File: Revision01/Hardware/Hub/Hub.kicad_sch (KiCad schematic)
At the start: 25 parts, among them J20 Conn_01x04, J3 Conn_01x04, J4 Conn_01x05, J5 Conn_01x05, SW1 ON/OFF_SW_SPST_LED, U1 NUCLEO-L476RG, U2 LMR51603XFDBVR

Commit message: . Fixed major BOM bug in Antenna, ordering correct Male Outer, Male Inner Part . Added Mouser column in Hub.
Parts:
- C2, C4: Mouser Link (none) -> https://www.mouser.ca/ProductDetail/Samsung-Electro-Mechani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; Mouser Part Number (none) -> 187-CL21B105KBFNNNE
- C3: Mouser Link (none) -> https://www.mouser.ca/ProductDetail/Samsung-Electro-Mechani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; Mouser Part Number (none) -> 187-CL21B104KCFNNNE
- C5: Mouser Link (none) -> https://www.mouser.ca/ProductDetail/Samsung-Electro-Mechani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; Mouser Part Number (none) -> 187-CL31B106KAHNNNE
- F1: Mouser Link (none) -> https://www.mouser.ca/ProductDetail/KYOCERA-AVX/F0603E0R37F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; Mouser Part Number (none) -> 581-F0603E0R37FSTR
- J20: now left out of the parts list
- L1: Mouser Link (none) -> https://www.mouser.ca/ProductDetail/Murata-Electronics/LQH4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; Mouser Part Number (none) -> 81-LQH44PH151MPRL
- N1: Mouser Link (none) -> https://www.mouser.ca/ProductDetail/Seeed-Studio/114090052?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; Mouser Part Number (none) -> 713-114090052
- R1: Manufacturer Part Number CRCW08050000Z0EAHP -> CRCW08050000Z0EA; Mouser Link (none) -> https://www.mouser.ca/ProductDetail/Vishay/CRCW08050000Z0EA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; Mouser Part Number (none) -> 71-CRCW0805-0-E3
- R3: Mouser Link (none) -> https://www.mouser.ca/ProductDetail/Vishay/CRCW080576K8FKEA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; Mouser Part Number (none) -> 71-CRCW080576K8FKEA
- R4: Mouser Link (none) -> https://www.mouser.ca/ProductDetail/Vishay/CRCW080510K0FKEA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; Mouser Part Number (none) -> 71-CRCW080510K0FKEAC
- SW1: Mouser Link (none) -> No Results; Mouser Part Number (none) -> No Results
- U1: Mouser Link (none) -> https://www.mouser.ca/ProductDetail/STMicroelectronics/NUCL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; Mouser Part Number (none) -> 511-NUCLEO-L476RG
- U2: Mouser Link (none) -> https://www.mouser.ca/ProductDetail/Texas-Instruments/LMR51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; Mouser Part Number (none) -> 595-LMR51606XDBVR
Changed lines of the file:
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@@
 			)
 		)
-		(property "Mouser Link" ""
+		(property "Mouser Link" "https://www.mouser.ca/ProductDetail/Samsung-Electro-Mechanics/CL21B105KBFNNNE?qs=yOVawPpwOwmddQEBPU6Y9A%3D%3D"
 			(at 137.16 92.71 0)
 			(effects
@@
 			)
 		)
-		(property "Mouser Part Number" ""
+		(property "Mouser Part Number" "187-CL21B105KBFNNNE "
 			(at 137.16 92.71 0)
 			(effects
@@
 			)
 		)
-		(property "Mouser Link" ""
+		(property "Mouser Link" "https://www.mouser.ca/ProductDetail/Vishay/CRCW080510K0FKEAC?qs=E3Y5ESvWgWORadmUijPtxQ%3D%3D"
 			(at 200.66 93.98 0)
 			(effects
@@
 			)
 		)
-		(property "Mouser Part Number" ""
+		(property "Mouser Part Number" "71-CRCW080510K0FKEAC"
 			(at 200.66 93.98 0)
 			(effects
@@
 			)
 		)
-		(property "Mouser Link" ""
+		(property "Mouser Link" "https://www.mouser.ca/ProductDetail/Samsung-Electro-Mechanics/CL31B106KAHNNNE?qs=349EhDEZ59r5EZhnLOTsYA%3D%3D"
 			(at 234.95 93.98 0)
 			(effects
@@
 			)
 		)
-		(property "Mouser Part Number" ""
+		(property "Mouser Part Number" "187-CL31B106KAHNNNE "
 			(at 234.95 93.98 0)
 			(effects
@@
 			)
 		)
-		(property "Mouser Link" ""
+		(property "Mouser Link" "https://www.mouser.ca/ProductDetail/STMicroelectronics/NUCLEO-L476RG?qs=PRtH0mD6DWbM6mRV5DKjBQ%3D%3D"
 			(at 115.57 209.55 0)
 			(effects
@@
 			)
 		)
-		(property "Mouser Part Number" ""
+		(property "Mouser Part Number" "511-NUCLEO-L476RG"
 			(at 115.57 209.55 0)
 			(effects
@@
 			)
 		)
-		(property "Mouser Link" ""
+		(property "Mouser Link" "https://www.mouser.ca/ProductDetail/Samsung-Electro-Mechanics/CL21B104KCFNNNE?qs=lptGheUA4EwiEGVRX9oguw%3D%3D"
 			(at 180.34 81.28 0)
 			(effects
@@
 			)
 		)
-		(property "Mouser Part Number" ""
+		(property "Mouser Part Number" "187-CL21B104KCFNNNE "
 			(at 180.34 81.28 0)
 			(effects
@@
 			)
 		)
-		(property "Mouser Link" ""
+		(property "Mouser Link" "https://www.mouser.ca/ProductDetail/Murata-Electronics/LQH44PH151MPRL?qs=rkhjVJ6%2F3EJ9BU%2FIW%252BFNJA%3D%3D"
 			(at 194.31 83.82 90)
 			(effects
@@
 			)
 		)
-		(property "Mouser Part Number" ""
+		(property "Mouser Part Number" "81-LQH44PH151MPRL"
 			(at 194.31 83.82 90)
 			(effects
@@
 			)
 		)
-		(property "Mouser Link" ""
+		(property "Mouser Link" "https://www.mouser.ca/ProductDetail/Texas-Instruments/LMR51606XDBVR?qs=mELouGlnn3eccxHdZD5yuw%3D%3D"
 			(at 142.24 78.74 0)
 			(effects
@@
 			)
 		)
-		(property "Mouser Part Number" ""
+		(property "Mouser Part Number" "595-LMR51606XDBVR"
 			(at 142.24 78.74 0)
 			(effects
@@
 			)
 		)
-		(property "Mouser Link" ""
+		(property "Mouser Link" "https://www.mouser.ca/ProductDetail/STMicroelectronics/NUCLEO-L476RG?qs=PRtH0mD6DWbM6mRV5DKjBQ%3D%3D"
 			(at 115.57 151.13 0)
 			(effects
@@
 			)
 		)
-		(property "Mouser Part Number" ""
+		(property "Mouser Part Number" "511-NUCLEO-L476RG"
 			(at 115.57 151.13 0)
 			(effects
@@
 			)
 		)
-		(property "Mouser Link" ""
+		(property "Mouser Link" "https://www.mouser.ca/ProductDetail/Vishay/CRCW080576K8FKEA?qs=Lu3mkJd%252BoBETDVTzIaHY%2FQ%3D%3D"
 			(at 200.66 86.36 0)
 			(effects
@@
 			)
 		)
-		(property "Mouser Part Number" ""
+		(property "Mouser Part Number" "71-CRCW080576K8FKEA"
 			(at 200.66 86.36 0)
 			(effects
@@
 			)
 		)
-		(property "Mouser Link" ""
+		(property "Mouser Link" "https://www.mouser.ca/ProductDetail/STMicroelectronics/NUCLEO-L476RG?qs=PRtH0mD6DWbM6mRV5DKjBQ%3D%3D"
 			(at 152.4 267.97 0)
 			(effects
@@
 			)
 		)
-		(property "Mouser Part Number" ""
+		(property "Mouser Part Number" "511-NUCLEO-L476RG"
 			(at 152.4 267.97 0)
 			(effects
@@
 			)
 		)
-		(property "Mouser Link" ""
+		(property "Mouser Link" "https://www.mouser.ca/ProductDetail/Seeed-Studio/114090052?qs=OTrKUuiFdkbetX%2F%2FZD%2Frtw%3D%3D"
 			(at 45.72 52.07 90)
 			(effects
@@
 			)
 		)
-		(property "Mouser Part Number" ""
+		(property "Mouser Part Number" "713-114090052"
 			(at 45.72 52.07 90)
 			(effects
@@
 			)
 		)
-		(property "Manufacturer Part Number" "CRCW08050000Z0EAHP"
+		(property "Manufacturer Part Number" "CRCW08050000Z0EA"
 			(at 118.11 66.04 0)
 			(effects
@@
 			)
 		)
-		(property "Mouser Link" ""
+		(property "Mouser Link" "https://www.mouser.ca/ProductDetail/Vishay/CRCW08050000Z0EA?qs=waxnFHLl2hB4NcTp6tAQPA%3D%3D"
 			(at 118.11 66.04 90)
 			(effects
@@
 			)
 		)
-		(property "Mouser Part Number" ""
+		(property "Mouser Part Number" "71-CRCW0805-0-E3"
 			(at 118.11 66.04 90)
 			(effects
@@
 			)
 		)
-		(property "Mouser Link" ""
+		(property "Mouser Link" "No Results"
 			(at 87.63 43.18 90)
 			(effects
@@
 			)
 		)
-		(property "Mouser Part Number" ""
+		(property "Mouser Part Number" "No Results"
 			(at 87.63 43.18 90)
 			(effects
@@
 		(unit 1)
 		(exclude_from_sim no)
-		(in_bom yes)
+		(in_bom no)
 		(on_board yes)
 		(dnp no)
@@
 			)
 		)
-		(property "Mouser Link" ""
+		(property "Mouser Link" "https://www.mouser.ca/ProductDetail/KYOCERA-AVX/F0603E0R37FSTR?qs=vco6xy%252BeH1oeD3dI3xk78w%3D%3D"
 			(at 71.12 66.04 0)
 			(effects
@@
 			)
 		)
-		(property "Mouser Part Number" ""
+		(property "Mouser Part Number" "581-F0603E0R37FSTR "
 			(at 71.12 66.04 0)
 			(effects
@@
 			)
 		)
-		(property "Mouser Link" ""
+		(property "Mouser Link" "https://www.mouser.ca/ProductDetail/Samsung-Electro-Mechanics/CL21B105KBFNNNE?qs=yOVawPpwOwmddQEBPU6Y9A%3D%3D"
 			(at 223.52 93.98 0)
 			(effects
@@
 			)
 		)
-		(property "Mouser Part Number" ""
+		(property "Mouser Part Number" "187-CL21B105KBFNNNE "
 			(at 223.52 93.98 0)
 			(effects

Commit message: . Exported BOM (.csv), gerbers & dill files, 3D Model (.step) file to Product/2025-08-16 for both Amplifier & Hub boards.
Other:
- company: BCIT BAJA -> BCIT Racing
- title: TELEMETRY SYSTEM -> Hub
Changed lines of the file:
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@@
 	(paper "A3")
 	(title_block
-		(title "TELEMETRY SYSTEM")
-		(date "2025-03-08")
-		(rev "A")
-		(company "BCIT BAJA")
+		(title "Hub")
+		(date "2025-08-16")
+		(rev "01")
+		(company "BCIT Racing")
+		(comment 1 "Parry Zhuo & Daniel Mahmoud")
 	)
 	(rectangle

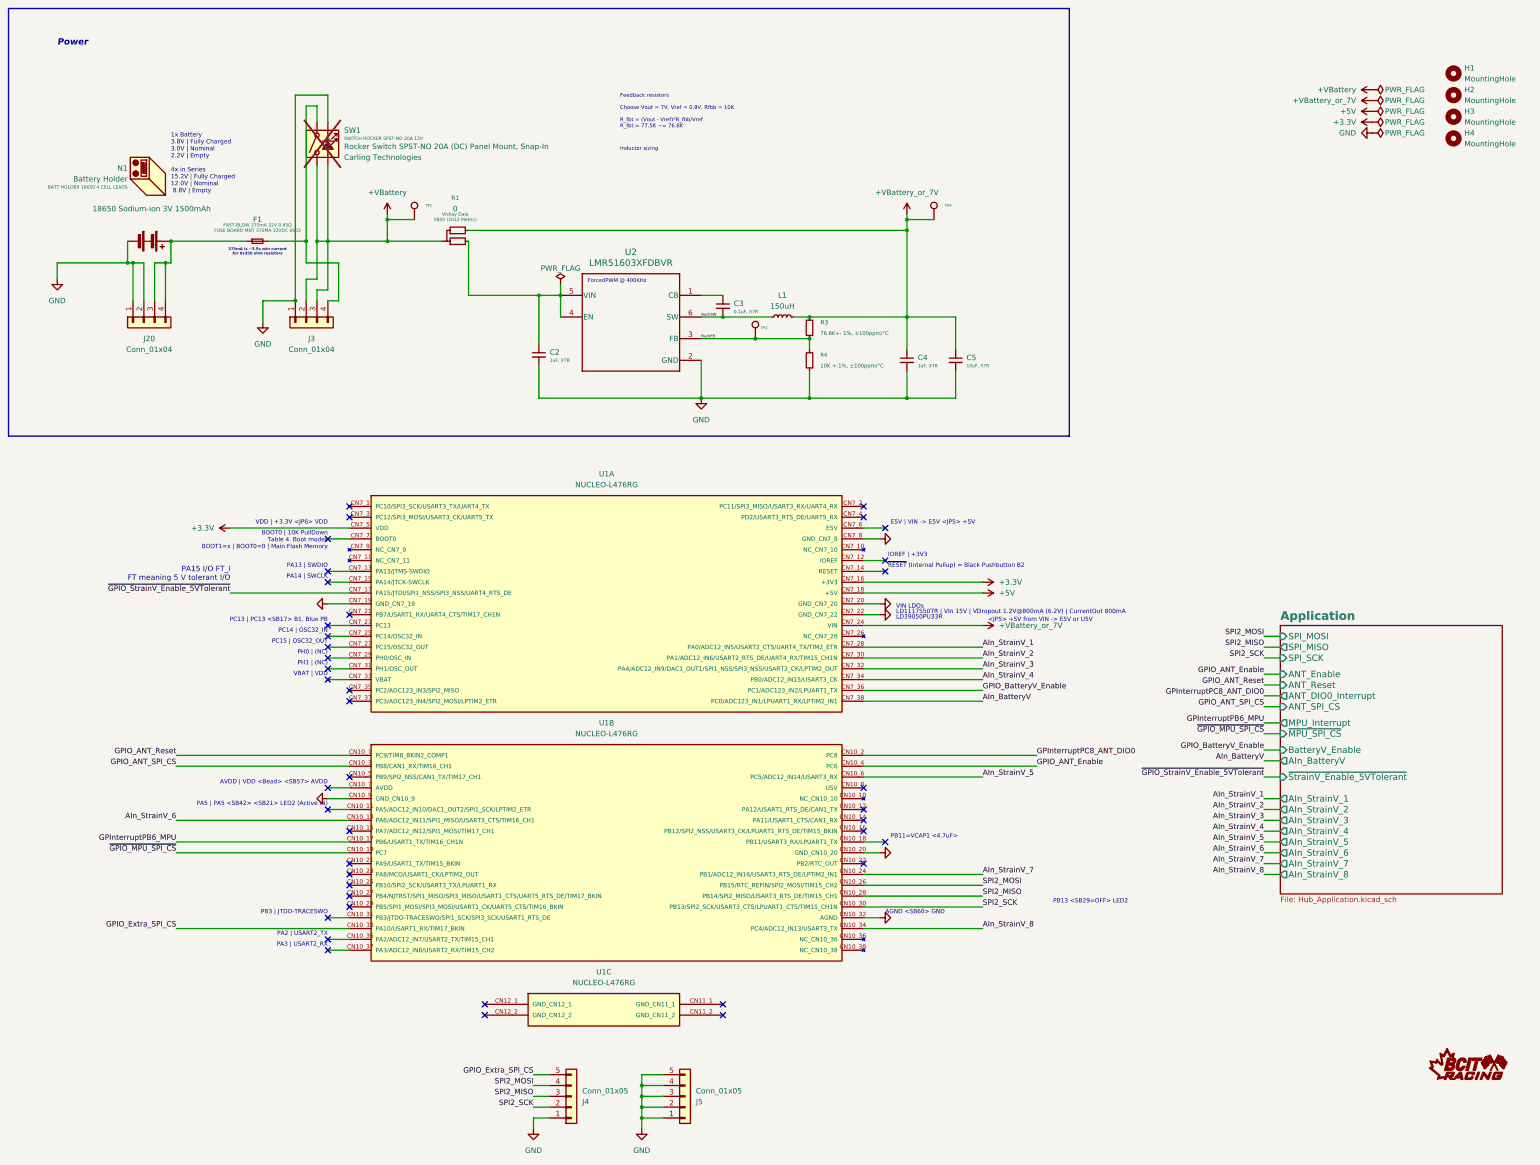
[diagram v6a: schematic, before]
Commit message: . Made sure amplifier passive silk screen doesn't overlap pads . Added 6xAA battery holder to hub BOM . Exported gerbers, drl files .zip (PCBWay approved)
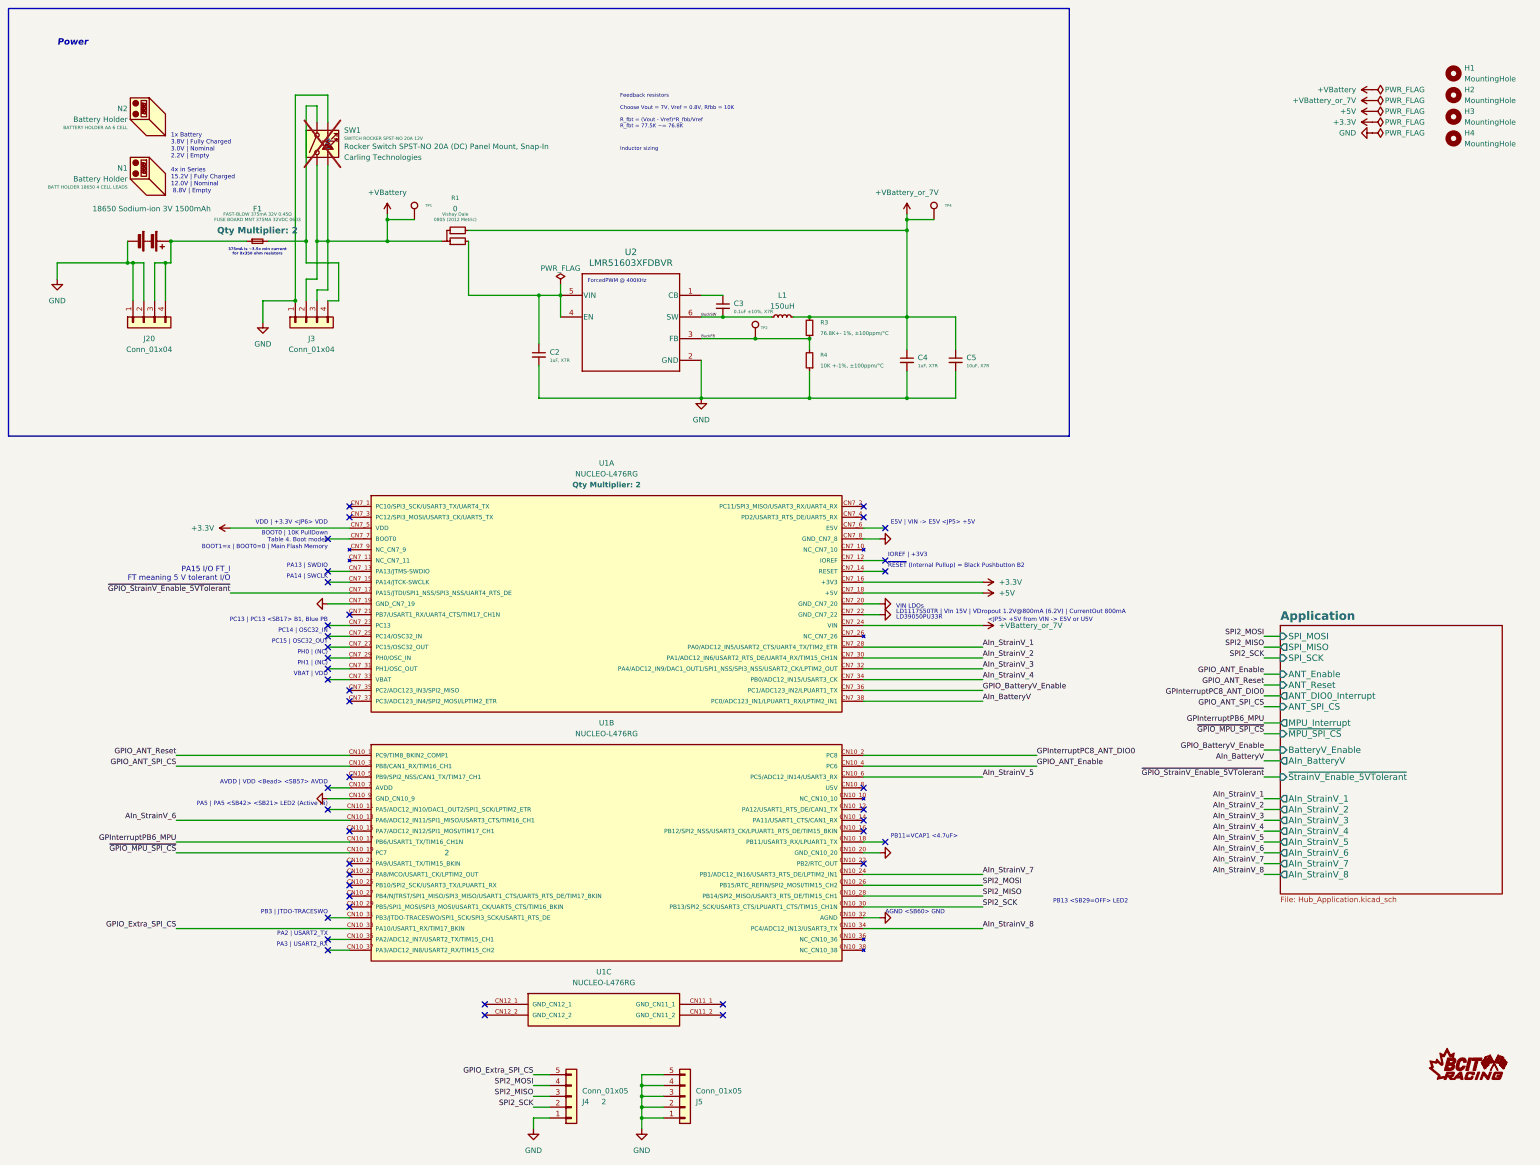
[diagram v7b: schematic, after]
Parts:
- added N2: Battery Holder, Lib:BATT_HOLDER_18650_4_CELL_LEADS, symbol Mechanical:Housing
- BT1: DigiKey Link https://www.aliexpress.com/item/1005005859082063.html -> (none)
- C2, C4: DigiKey Part Number 1276-1029-1-ND - Cut Tape (CT) -> 1276-1029-1-ND
- C3: value 0.1µF, X7R -> 0.1uF ±10%, X7R; DigiKey Part Number 1276-6840-1-ND - Cut Tape (CT) -> 1276-6840-1-ND
- C5: DigiKey Part Number 1276-1804-1-ND - Cut Tape (CT) -> 1276-1804-1-ND
- F1: DigiKey Part Number 478-2859-1-ND - Cut Tape (CT) -> 478-2859-1-ND; Qty Multiplier (none) -> 2
- L1: DigiKey Part Number 490-LQH44PH151MPRLCT-ND - Cut Tape (CT) -> 490-LQH44PH151MPRLCT-ND
- R1: DigiKey Part Number 541-0.0TBCT-ND - Cut Tape (CT) -> 541-0.0TBCT-ND
- R3: DigiKey Part Number 541-76.8KCCT-ND - Cut Tape (CT) -> 541-76.8KCCT-ND
- R4: DigiKey Part Number 541-3976-1-ND - Cut Tape (CT) -> 541-3976-1-ND
- U1: Qty Multiplier (none) -> 2
- U2: DigiKey Part Number 296-LMR51606XDBVRCT-ND - Cut Tape (CT) -> 296-LMR51606XDBVRCT-ND
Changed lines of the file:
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@@
 			)
 		)
-		(property "DigiKey Part Number" "1276-1029-1-ND - Cut Tape (CT)"
+		(property "DigiKey Part Number" "1276-1029-1-ND "
 			(at 137.16 92.71 0)
 			(effects
@@
 	)
 	(symbol
+		(lib_id "Mechanical:Housing")
+		(at 45.72 38.1 270)
+		(unit 1)
+		(exclude_from_sim yes)
+		(in_bom yes)
+		(on_board no)
+		(dnp no)
+		(fields_autoplaced yes)
+		(property "Reference" "N2"
+			(at 40.64 34.9249 90)
+			(effects
+				(font
+					(size 1.27 1.27)
+				)
+				(justify right)
+			)
+		)
+		(property "Value" "Battery Holder"
+			(at 40.64 37.4649 90)
+			(effects
+				(font
+					(size 1.27 1.27)
+				)
+				(justify right)
+			)
+		)
+		(property "Footprint" "Lib:BATT_HOLDER_18650_4_CELL_LEADS"
+			(at 46.99 39.37 0)
+			(effects
+				(font
+					(size 1.27 1.27)
+				)
+				(hide yes)
+			)
+		)
+		(property "Datasheet" "https://www.memoryprotectiondevices.com/datasheets/BH26AAB/BH26AAB-datasheet.pdf"
+			(at 46.99 39.37 0)
+			(effects
+				(font
+					(size 1.27 1.27)
+				)
+				(hide yes)
+			)
+		)
+		(property "Description" "BATTERY HOLDER AA 6 CELL"
+			(at 40.64 39.37 90)
+			(effects
+				(font
+					(size 0.762 0.762)
+				)
+				(justify right)
+			)
+		)
+		(property "Manufacturer" "MPD (Memory Protection Devices)"
+			(at 40.64 38.0999 90)
+			(effects
+				(font
+					(size 1.27 1.27)
+				)
+				(justify right)
+				(hide yes)
+			)
+		)
+		(property "Manufacturer Part Number" "BH26AAB"
+			(at 40.64 40.6399 90)
+			(effects
+				(font
+					(size 1.27 1.27)
+				)
+				(justify right)
+				(hide yes)
+			)
+		)
+		(property "Qty Multiplier" ""
+			(at 45.72 38.1 0)
+			(effects
+				(font
+					(size 1.27 1.27)
+				)
+			)
+		)
+		(property "Detailed Description" "Battery Holder (Covered) AA 6 Cell"
+			(at 45.72 38.1 0)
+			(effects
+				(font
+					(size 1.27 1.27)
+				)
+				(hide yes)
+			)
+		)
+		(property "Package" "n/a"
+			(at 45.72 38.1 0)
+			(effects
+				(font
+					(size 1.27 1.27)
+				)
+				(hide yes)
+			)
+		)
+		(property "DigiKey Link" "https://www.digikey.ca/en/products/detail/mpd-memory-protection-devices/BH26AAB/2439329?s=N4IgTCBcDaILIAUAiACAQgCTANgIK7RAF0BfIA"
+			(at 45.72 38.1 90)
+			(effects
+				(font
+					(size 1.27 1.27)
+				)
+				(hide yes)
+			)
+		)
+		(property "DigiKey Part Number" "BH26AAB-ND"
+			(at 45.72 38.1 90)
+			(effects
+				(font
+					(size 1.27 1.27)
+				)
+				(hide yes)
+			)
+		)
+		(property "AliExpress Link" ""
+			(at 45.72 38.1 90)
+			(effects
+				(font
+					(size 1.27 1.27)
+				)
+				(hide yes)
+			)
+		)
+		(property "AliExpress Part Number" ""
+			(at 45.72 38.1 90)
+			(effects
+				(font
+					(size 1.27 1.27)
+				)
+				(hide yes)
+			)
+		)
+		(property "Mouser Link" ""
+			(at 45.72 38.1 90)
+			(effects
+				(font
+					(size 1.27 1.27)
+				)
+				(hide yes)
+			)
+		)
+		(property "Mouser Part Number" ""
+			(at 45.72 38.1 90)
+			(effects
+				(font
+					(size 1.27 1.27)
+				)
+				(hide yes)
+			)
+		)
+		(instances
+			(project "Hub"
+				(path "/955cc99e-a129-42cf-abc7-aa99813fdb5f"
+					(reference "N2")
+					(unit 1)
+				)
+			)
+		)
+	)
+	(symbol
 		(lib_id "power:GND")
 		(at 87.63 151.13 270)
@@
 			)
 		)
-		(property "DigiKey Part Number" "541-3976-1-ND - Cut Tape (CT)"
+		(property "DigiKey Part Number" "541-3976-1-ND "
 			(at 200.66 93.98 0)
 			(effects
@@
 			)
 		)
-		(property "DigiKey Part Number" "1276-1804-1-ND - Cut Tape (CT)"
+		(property "DigiKey Part Number" "1276-1804-1-ND "
 			(at 234.95 93.98 0)
 			(effects
@@
 			)
 		)
-		(property "Qty Multiplier" ""
+		(property "Qty Multiplier" "2"
 			(at 115.57 209.55 0)
 			(effects
@@
 			)
 		)
-		(property "Value" "0.1µF, X7R"
+		(property "Value" "0.1uF ±10%, X7R"
 			(at 182.88 82.55 0)
 			(effects
@@
 			)
 		)
-		(property "DigiKey Part Number" "1276-6840-1-ND - Cut Tape (CT)"
+		(property "DigiKey Part Number" "1276-6840-1-ND "
 			(at 180.34 81.28 0)
 			(effects
@@
 			)
 		)
-		(property "DigiKey Part Number" "490-LQH44PH151MPRLCT-ND - Cut Tape (CT)"
+		(property "DigiKey Part Number" "490-LQH44PH151MPRLCT-ND "
 			(at 194.31 83.82 90)
 			(effects
@@
 			)
 		)
-		(property "DigiKey Part Number" "296-LMR51606XDBVRCT-ND - Cut Tape (CT)"
+		(property "DigiKey Part Number" "296-LMR51606XDBVRCT-ND "
 			(at 142.24 78.74 0)
 			(effects
@@
 		(fields_autoplaced yes)
 		(property "Reference" "U1"
-			(at 153.035 120.65 0)
+			(at 153.035 118.11 0)
 			(effects
 				(font
@@
 		)
 		(property "Value" "NUCLEO-L476RG"
-			(at 153.035 123.19 0)
+			(at 153.035 120.65 0)
 			(effects
 				(font
@@
 			)
 		)
-		(property "Qty Multiplier" ""
-			(at 115.57 151.13 0)
+		(property "Qty Multiplier" "2"
+			(at 153.035 123.19 0)
+			(show_name yes)
 			(effects
 				(font
 					(size 1.27 1.27)
+					(thickness 0.254)
+					(bold yes)
 				)
 			)
@@
 			)
 		)
-		(property "DigiKey Part Number" "541-76.8KCCT-ND - Cut Tape (CT)"
+		(property "DigiKey Part Number" "541-76.8KCCT-ND "
 			(at 200.66 86.36 0)
 			(effects
@@
 			)
 		)
+		(property "Qty Multiplier" "2"
+			(at 152.4 267.97 0)
+			(effects
+				(font
+					(size 1.27 1.27)
+				)
+			)
+		)
 		(pin "CN7_17"
 		)
@@
 			)
 		)
-		(property "DigiKey Link" "https://www.aliexpress.com/item/1005005859082063.html"
+		(property "DigiKey Link" ""
 			(at 45.72 66.04 0)
 			(effects
@@
 			)
 		)
-		(property "DigiKey Part Number" "541-0.0TBCT-ND - Cut Tape (CT)"
+		(property "DigiKey Part Number" "541-0.0TBCT-ND "
 			(at 118.11 66.04 90)
 			(effects
@@
 		(fields_autoplaced yes)
 		(property "Reference" "F1"
-			(at 71.12 60.96 0)
+			(at 71.12 58.42 0)
 			(effects
 				(font
@@
 		)
 		(property "Value" "FAST-BLOW 375mA 32V 0.45Ω"
-			(at 71.12 62.23 0)
+			(at 71.12 59.69 0)
 			(effects
 				(font
@@
 		)
 		(property "Description" "FUSE BOARD MNT 375MA 32VDC 0603"
-			(at 71.12 63.5 0)
+			(at 71.12 60.96 0)
 			(effects
 				(font
@@
 			)
 		)
-		(property "DigiKey Part Number" "478-2859-1-ND - Cut Tape (CT)"
+		(property "DigiKey Part Number" "478-2859-1-ND "
 			(at 71.12 66.04 0)
 			(effects
@@
 			)
 		)
+		(property "Qty Multiplier" "2"
+			(at 71.12 63.5 0)
+			(show_name yes)
+			(effects
+				(font
+					(size 1.4986 1.4986)
+					(thickness 0.2997)
+					(bold yes)
+				)
+			)
+		)
 		(pin "2"
 		)
@@
 			)
 		)
-		(property "DigiKey Part Number" "1276-1029-1-ND - Cut Tape (CT)"
+		(property "DigiKey Part Number" "1276-1029-1-ND "
 			(at 223.52 93.98 0)
 			(effects
